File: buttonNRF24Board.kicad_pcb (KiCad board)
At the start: 2 copper layers, 44.7 x 25 mm, 22 parts, among them J1 INTERFACE, U1 NRF24L01, X1 16MHz

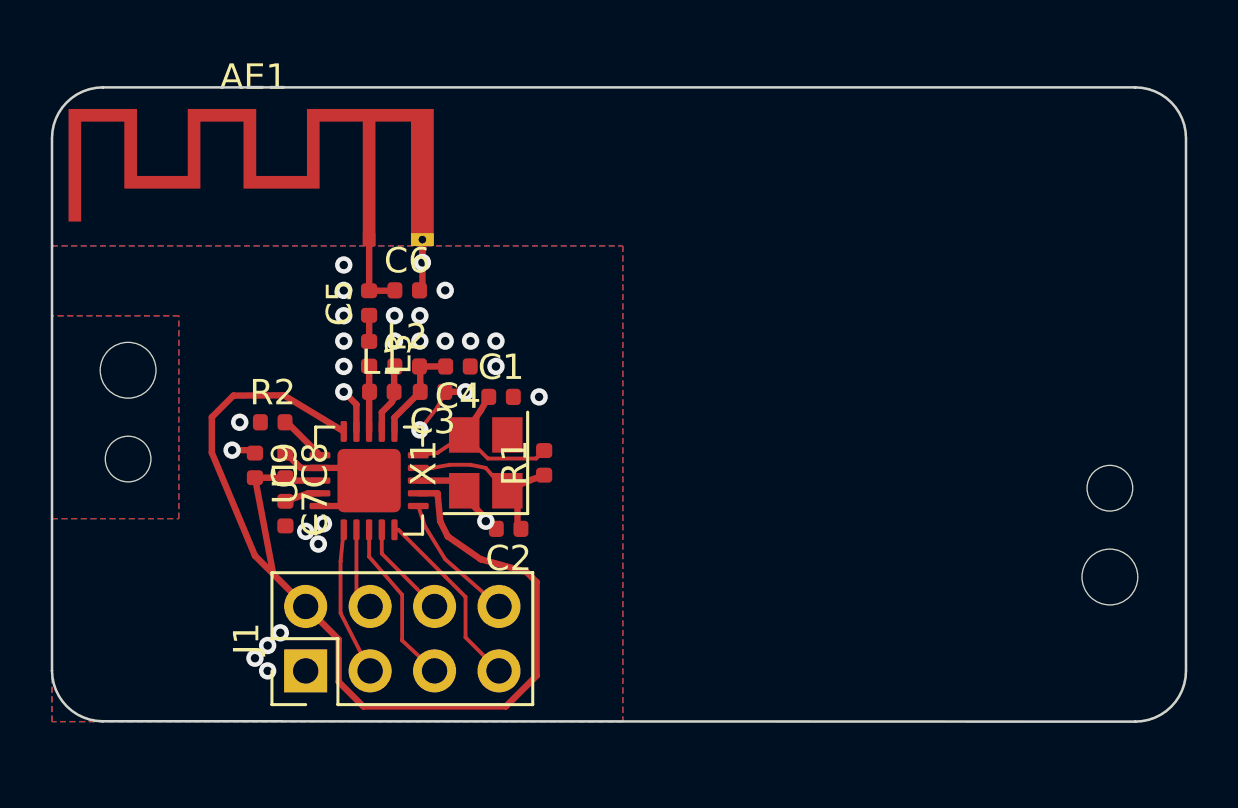
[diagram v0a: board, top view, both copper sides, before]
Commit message: Tweaking board shape and traces
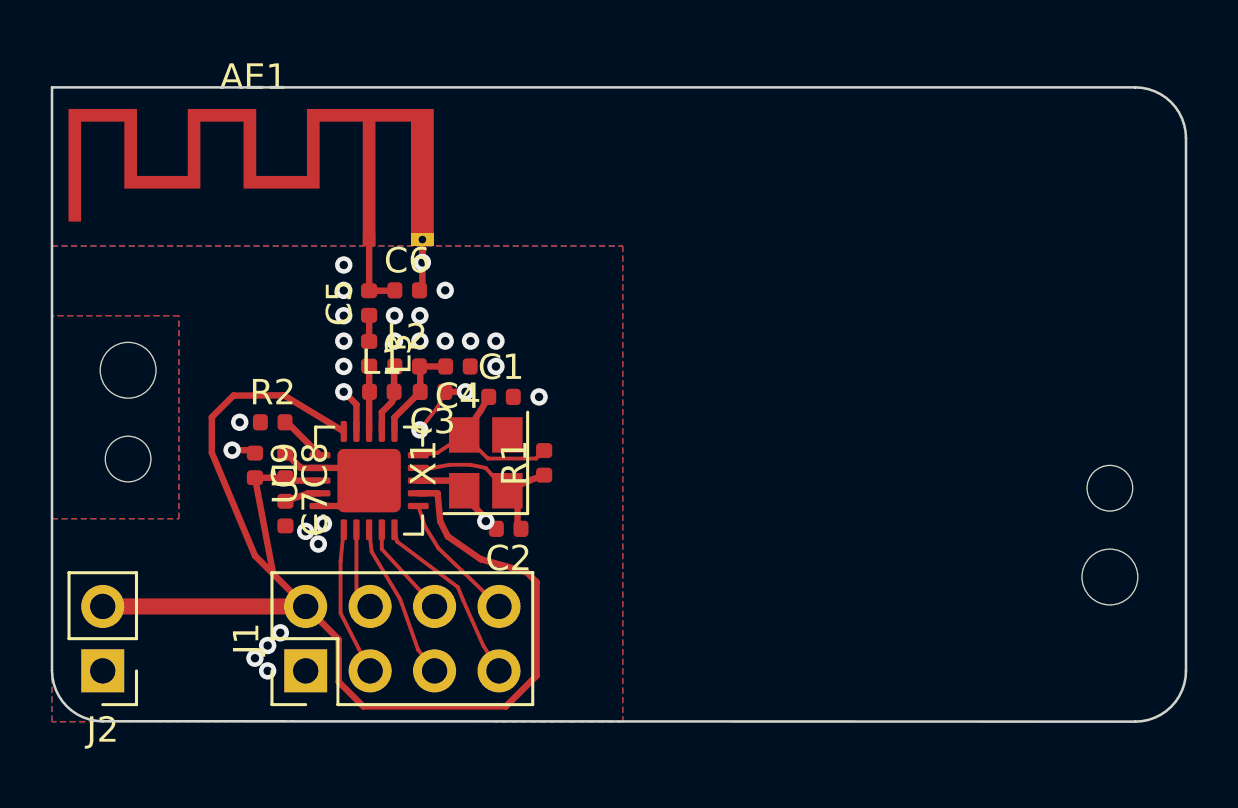
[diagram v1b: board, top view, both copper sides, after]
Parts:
- added J2: 2SAA, Connector_PinHeader_2.54mm:PinHeader_1x02_P2.54mm_Vertical, F.Cu at (42.0, 113.0)
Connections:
- net GND renamed EP
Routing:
- net VDD: track 43.5 -> 51.5 mm
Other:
- outline, holes or cut-outs redrawn
